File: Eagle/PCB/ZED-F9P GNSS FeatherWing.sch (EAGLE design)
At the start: 41 parts, among them U1 ZED-F9P_ZED-F9P, U2 SPX3819-3.3, X1 SMA-142-0711-821/826

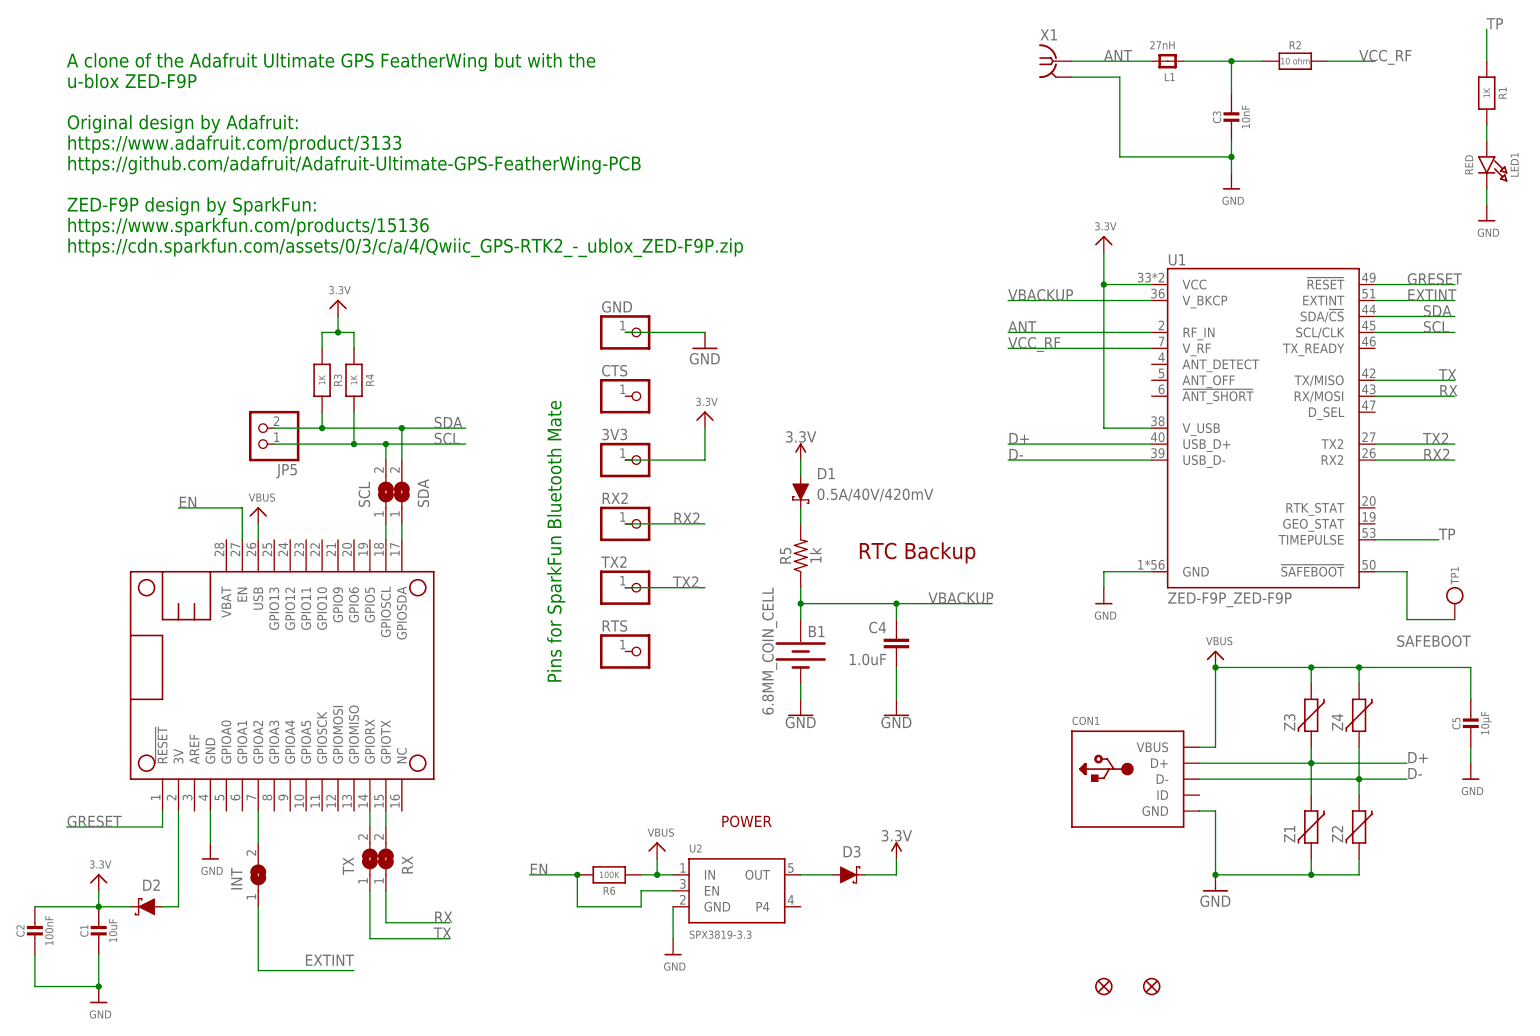
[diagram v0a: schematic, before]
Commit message: Updated the power circuit
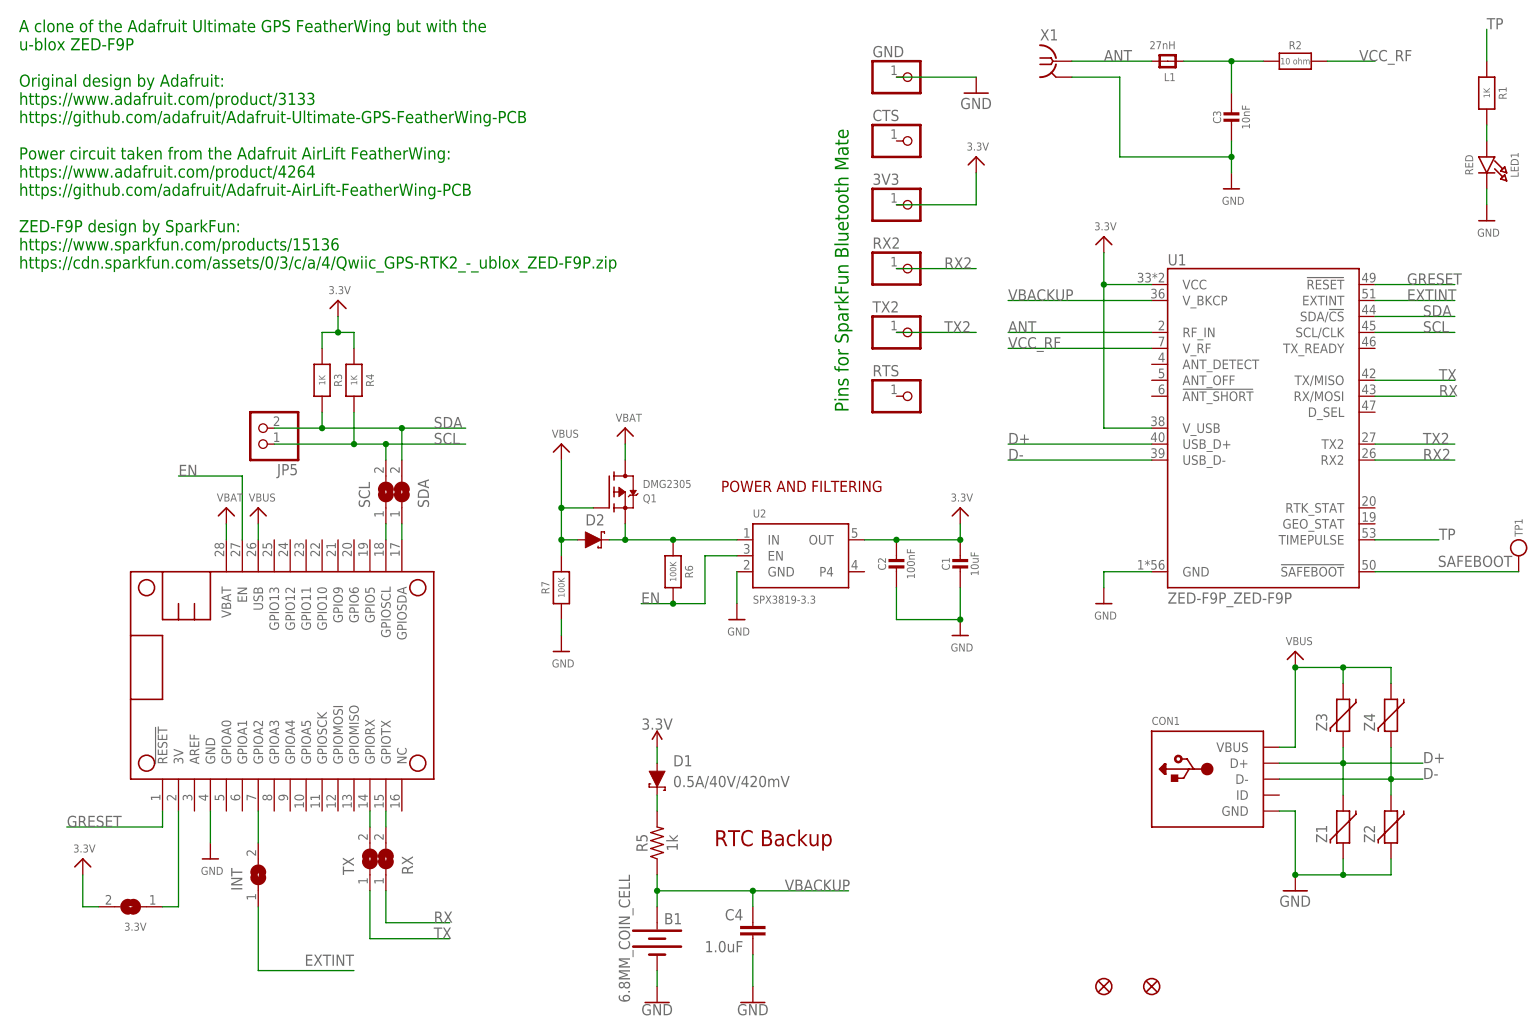
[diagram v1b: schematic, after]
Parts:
- removed C5: 10µF, microbuilder:CAP_CERAMIC0805-NOOUTLINE
- removed D3: 0.5A/40V/420mV, SparkFun-DiscreteSemi:DIODE-SCHOTTKY-PMEG4005EJ
- added 3.3V: (no value), microbuilder:SOLDERJUMPER
- added Q1: DMG2305, microbuilder:MOSFET-P
- added R7: 100K, microbuilder:RESISTOR_0603_NOOUT
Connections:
- removed net OUT: D3.A, U2.OUT
- new net N$10: D2.C, Q1.S, R6.1, U2.IN
- new net VBAT: MS1.VBAT, Q1.D
- net 3.3V: now also 3.3V.2, U2.OUT; no longer D2.C, D3.C
- net 3V: now also 3.3V.1; no longer D2.A
- net GND: now also R7.1; no longer C5.2
- net VBUS: now also D2.A, Q1.G, R7.2; no longer C5.1, R6.1, U2.IN
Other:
- note added: "A clone of the Adafruit Ultimate GPS FeatherWing but with the u-blox ZED-F9P Original design by Adafruit: https://www.adafruit.com/product/3133 https://github.com/adafruit/Adafruit-Ultimate-GPS-FeatherWing-PCB Power circuit taken from the Adafruit AirLift FeatherWing: https://www.adafruit.com/product/4264 https://github.com/adafruit/Adafruit-AirLift-FeatherWing-PCB ZED-F9P design by SparkFun: htt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"
- note added: "POWER AND FILTERING"
- note removed: "A clone of the Adafruit Ultimate GPS FeatherWing but with the u-blox ZED-F9P Original design by Adafruit: https://www.adafruit.com/product/3133 https://github.com/adafruit/Adafruit-Ultimate-GPS-FeatherWing-PCB ZED-F9P design by SparkFun: https://www.sparkfun.com/products/15136 https://cdn.sparkfun.com/assets/0/3/c/a/4/Qwiic_GPS-RTK2_-_ublox_ZED-F9P.zip"
- note removed: "POWER"
- moved on the sheet: 3V3, B1, C1, C2, C4, CON1, CTS, D1, D2, GND, R5, R6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

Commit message: Ready for manufacture
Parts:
- renumbered LED1 to PPS
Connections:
- net GRESET renamed !RESET
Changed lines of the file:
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@@
 </classes>
 <parts>
-<part name="LED1" library="microbuilder" deviceset="LED" device="0805_NOOUTLINE" value="RED"/>
+<part name="PPS" library="microbuilder" deviceset="LED" device="0805_NOOUTLINE" value="RED"/>
 <part name="U$3" library="microbuilder" deviceset="3.3V" device=""/>
 <part name="U$4" library="microbuilder" deviceset="3.3V" device=""/>
@@
 </plain>
 <instances>
-<instance part="LED1" gate="G$1" x="243.84" y="144.78" smashed="yes" rot="R270">
+<instance part="PPS" gate="G$1" x="243.84" y="144.78" smashed="yes" rot="R270">
 <attribute name="NAME" x="248.285" y="146.05" size="1.27" layer="95" rot="R270" align="center"/>
 <attribute name="VALUE" x="241.046" y="146.05" size="1.27" layer="96" rot="R270" align="center"/>
@@
 <segment>
 <pinref part="U$13" gate="G$1" pin="GND"/>
-<pinref part="LED1" gate="G$1" pin="C"/>
+<pinref part="PPS" gate="G$1" pin="C"/>
 <wire x1="243.84" y1="139.7" x2="243.84" y2="142.24" width="0.1524" layer="91"/>
 </segment>
@@
 </segment>
 </net>
-<net name="GRESET" class="0">
+<net name="!RESET" class="0">
 <segment>
 <label x="17.78" y="40.64" size="1.778" layer="95"/>
@@
 <net name="N$2" class="0">
 <segment>
-<pinref part="LED1" gate="G$1" pin="A"/>
+<pinref part="PPS" gate="G$1" pin="A"/>
 <wire x1="243.84" y1="149.86" x2="243.84" y2="152.4" width="0.1524" layer="91"/>
 <pinref part="R1" gate="G$1" pin="2"/>
